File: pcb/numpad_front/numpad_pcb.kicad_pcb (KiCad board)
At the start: 2 copper layers, 81 x 160.2 mm, 63 parts, among them J1 Conn_01x16_Female

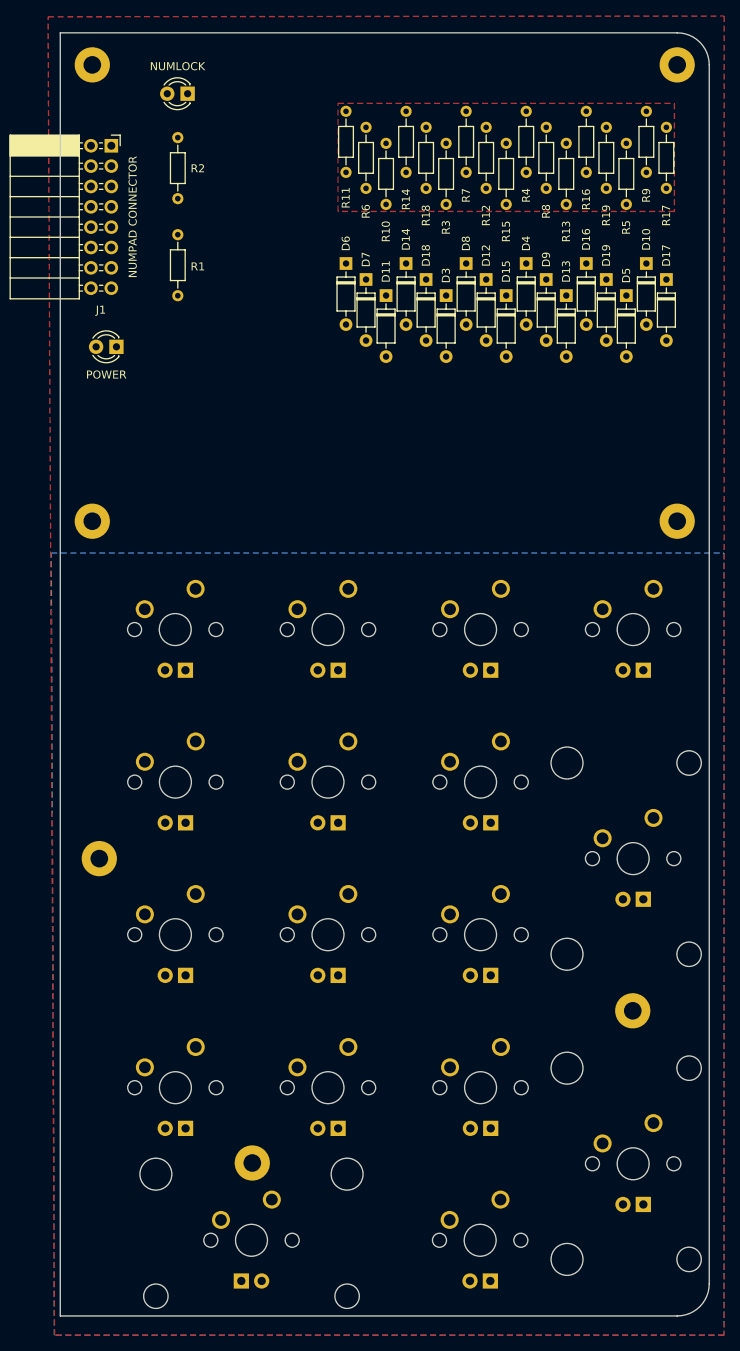
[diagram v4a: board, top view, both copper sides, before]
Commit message: Finish numpad routing
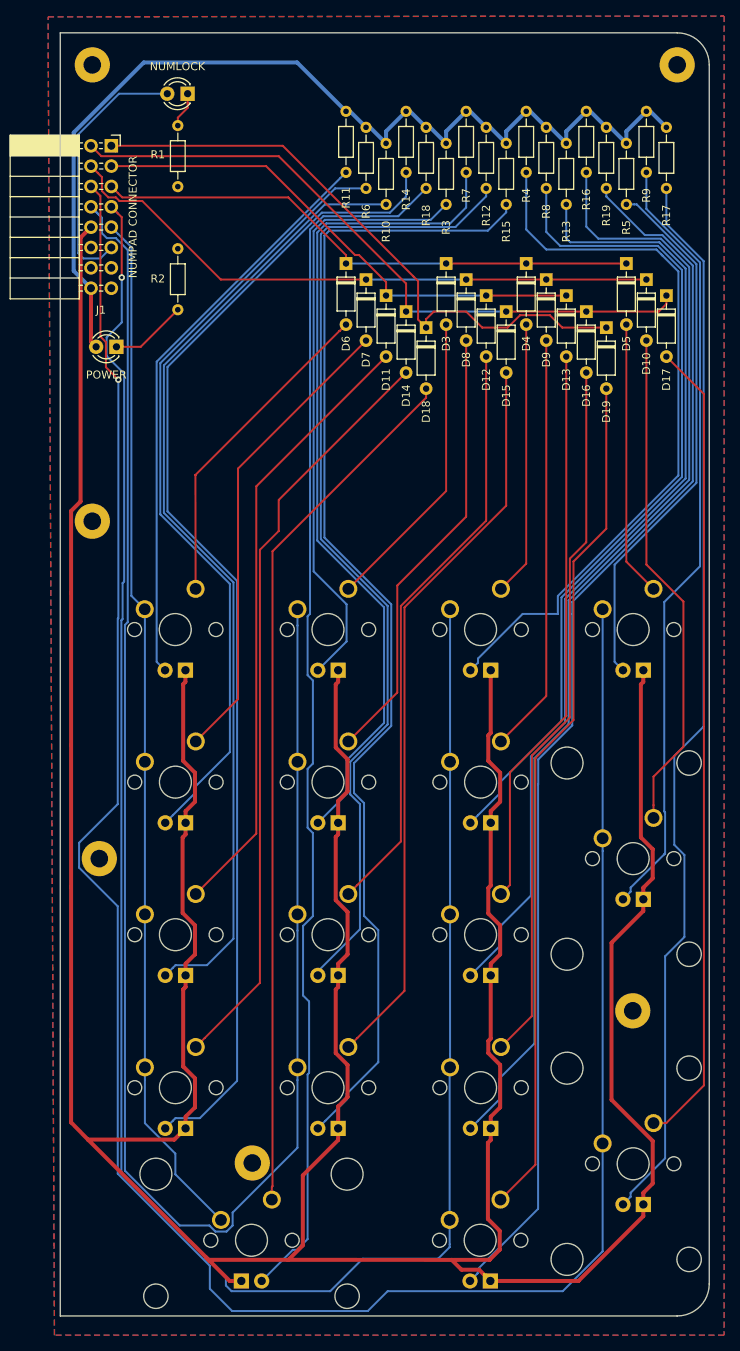
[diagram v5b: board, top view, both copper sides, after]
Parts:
- removed the REF** at (67.5, 87.0) (x2)
- added REF**: MountingHole_2.2mm_M2_Pad, MountingHole:MountingHole_2.2mm_M2_Pad, F.Cu at (67.5, 87.0)
- moved R2 6.25 mm to (78.2, 53.0), turned to 270 degrees
- moved D14 6.00 mm to (106.7, 60.8)
- moved D16 6.00 mm to (129.2, 60.8)
- moved D18 6.00 mm to (109.2, 62.8)
- moved D19 6.00 mm to (131.7, 62.8)
- moved R1 6.00 mm to (78.2, 45.2), turned to 90 degrees
- moved D3 4.00 mm to (111.7, 54.8)
- moved D5 4.00 mm to (134.2, 54.8)
- moved D10 2.00 mm to (136.7, 56.8)
- moved D12 2.00 mm to (116.7, 58.8)
- moved D15 2.00 mm to (119.2, 60.8)
- moved D17 2.00 mm to (139.2, 58.8)
- moved D8 2.00 mm to (114.2, 56.8)
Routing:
- net LEDGND: track 0.00 -> 511.9 mm
- net col19: track 0.00 -> 281.3 mm, vias 0 -> 1
- net col18: track 0.00 -> 253.9 mm, vias 0 -> 1
- net col17: track 0.00 -> 221.9 mm
- net Net-(MX17-Pad3): track 0.00 -> 153.7 mm
- net Net-(MX16-Pad3): track 0.00 -> 152.4 mm
- net Net-(MX13-Pad3): track 0.00 -> 146.1 mm
- net Net-(MX12-Pad3): track 0.00 -> 145.8 mm
- net Net-(MX14-Pad3): track 0.00 -> 140.6 mm
- net Net-(MX15-Pad3): track 0.00 -> 134.0 mm
- net +5V: track 0.00 -> 129.9 mm
- net col16: track 0.00 -> 129.7 mm
- net Net-(MX10-Pad3): track 0.00 -> 124.2 mm
- net Net-(MX9-Pad3): track 0.00 -> 121.7 mm
- net Net-(MX11-Pad3): track 0.00 -> 120.1 mm
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- added copper zone on B.Cu, net GND
- removed copper zone on F.Cu, net +5V
- removed copper zone on B.Cu, net LEDGND
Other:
- net class PWR added: clearance 0.2, trace_width 0.5, via_dia 0.8, via_drill 0.4

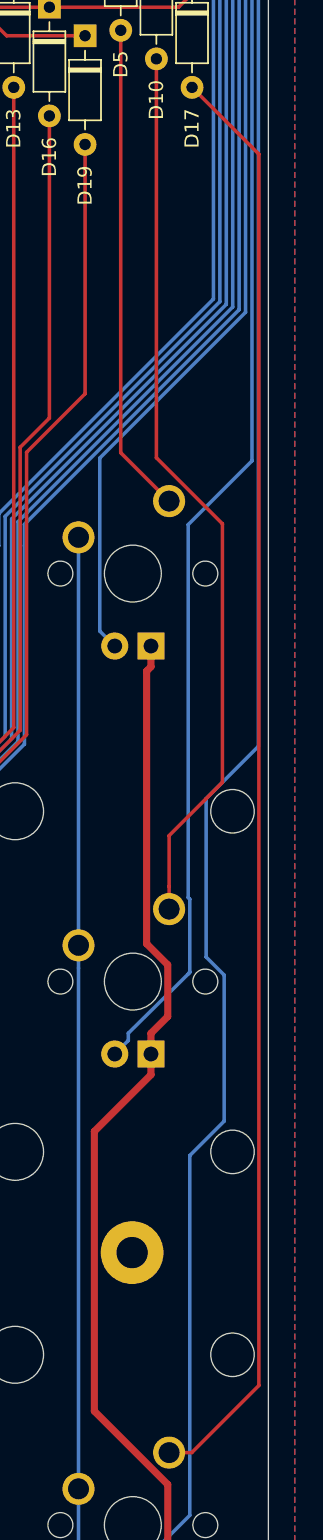
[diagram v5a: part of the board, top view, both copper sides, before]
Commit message: Rearrange main board diodes
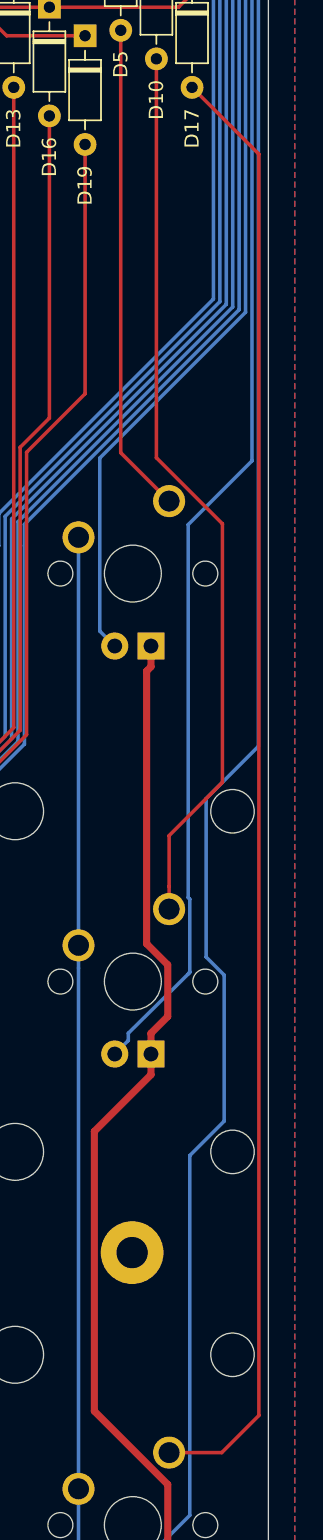
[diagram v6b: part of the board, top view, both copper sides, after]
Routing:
- net Net-(D17-Pad2): track 101.2 -> 102.4 mm
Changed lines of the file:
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@@
   (segment (start 127.15001 91.64999) (end 127.150009 111.486401) (width 0.25) (layer F.Cu) (net 22))
   (segment (start 127.150009 111.486401) (end 122.4 116.23641) (width 0.25) (layer F.Cu) (net 22))
-  (segment (start 139.18099 162.12) (end 137.59 162.12) (width 0.25) (layer F.Cu) (net 23))
-  (segment (start 143.884001 71.104001) (end 143.884001 157.416989) (width 0.25) (layer F.Cu) (net 23))
-  (segment (start 143.884001 157.416989) (end 139.18099 162.12) (width 0.25) (layer F.Cu) (net 23))
-  (segment (start 139.2 66.42) (end 143.884001 71.104001) (width 0.25) (layer F.Cu) (net 23))
+  (segment (start 143.884001 71.104001) (end 139.2 66.42) (width 0.25) (layer F.Cu) (net 23))
+  (segment (start 137.59 162.12) (end 141.28 162.12) (width 0.25) (layer F.Cu) (net 23))
+  (segment (start 143.884001 159.515999) (end 143.884001 71.104001) (width 0.25) (layer F.Cu) (net 23))
+  (segment (start 141.28 162.12) (end 143.884001 159.515999) (width 0.25) (layer F.Cu) (net 23))
   (segment (start 109.2 71.55137) (end 90.025001 90.726369) (width 0.25) (layer F.Cu) (net 24))
   (segment (start 109.2 70.42) (end 109.2 71.55137) (width 0.25) (layer F.Cu) (net 24))

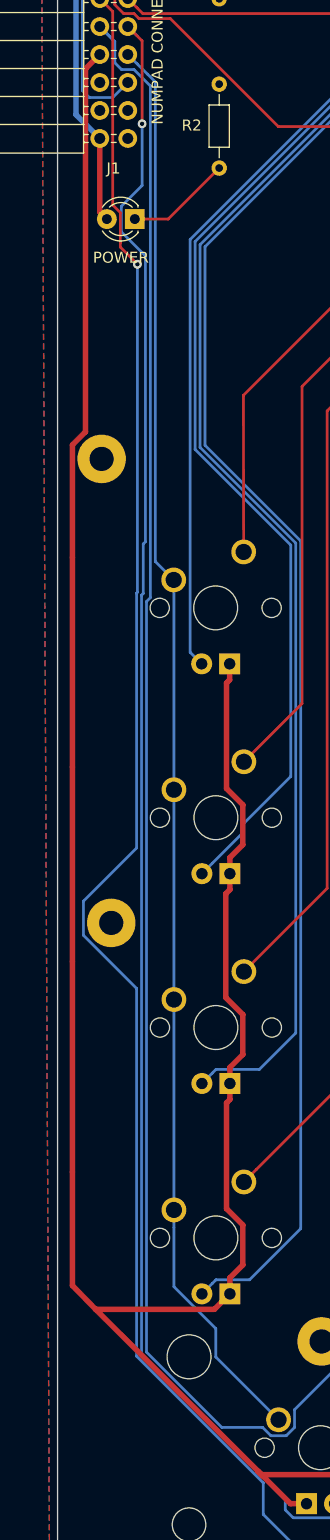
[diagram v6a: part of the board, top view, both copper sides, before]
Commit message: Finish routing main PCB
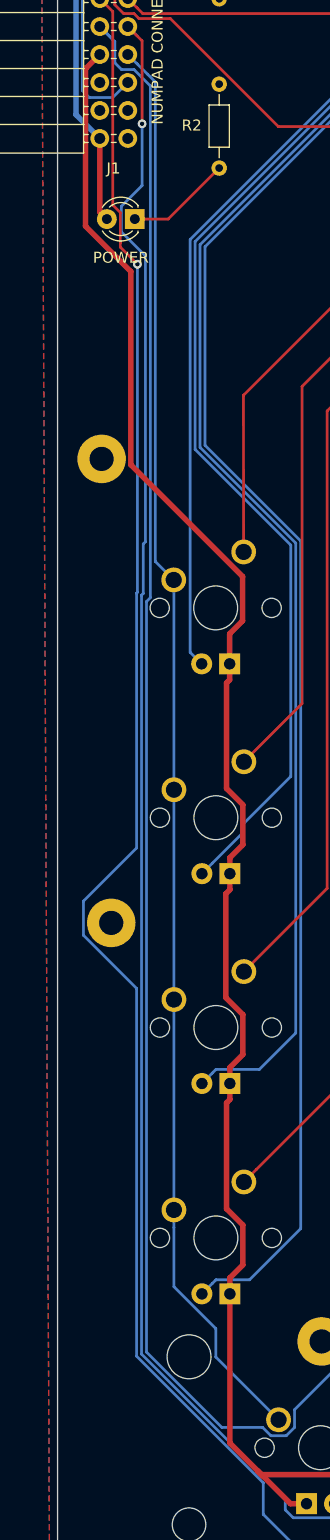
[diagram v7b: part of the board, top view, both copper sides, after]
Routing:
- net LEDGND: track 511.9 -> 441.9 mm
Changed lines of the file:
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@@
     (thickness 1.6)
     (drawings 8)
-    (tracks 579)
+    (tracks 576)
     (zones 0)
     (modules 62)
@@
   (segment (start 122.85001 167.30999) (end 118.49 171.67) (width 0.25) (layer F.Cu) (net 26))
   (segment (start 122.85001 116.54999) (end 122.85001 167.30999) (width 0.25) (layer F.Cu) (net 26))
-  (segment (start 64.874999 85.702999) (end 64.874999 95.920701) (width 0.5) (layer F.Cu) (net 31))
-  (segment (start 66.059999 84.517999) (end 64.874999 85.702999) (width 0.5) (layer F.Cu) (net 31))
-  (segment (start 66.059999 51.560001) (end 66.059999 84.517999) (width 0.5) (layer F.Cu) (net 31))
   (segment (start 67.36 50.26) (end 66.059999 51.560001) (width 0.5) (layer F.Cu) (net 31))
-  (segment (start 64.874999 95.920701) (end 64.874999 114.950701) (width 0.5) (layer F.Cu) (net 31))
-  (segment (start 64.874999 132.616001) (end 64.874999 114.950701) (width 0.5) (layer F.Cu) (net 31))
-  (segment (start 64.874999 132.616001) (end 64.874999 151.716001) (width 0.5) (layer F.Cu) (net 31))
   (segment (start 84.6775 181.83) (end 86.13 181.83) (width 0.5) (layer F.Cu) (net 31))
-  (segment (start 64.874999 151.716001) (end 64.874999 162.027499) (width 0.5) (layer F.Cu) (net 31))
   (segment (start 82.17375 179.32625) (end 84.6775 181.83) (width 0.5) (layer F.Cu) (net 31))
   (segment (start 79.17 123.1775) (end 79.17 124.63) (width 0.5) (layer F.Cu) (net 31))
@@
   (segment (start 136.32 170.8275) (end 137.493901 169.653599) (width 0.5) (layer F.Cu) (net 31))
   (segment (start 136.32 172.28) (end 136.32 170.8275) (width 0.5) (layer F.Cu) (net 31))
-  (segment (start 67.017499 164.182501) (end 67 164.2) (width 0.5) (layer F.Cu) (net 31))
-  (segment (start 79.17 162.78) (end 77.767499 164.182501) (width 0.5) (layer F.Cu) (net 31))
-  (segment (start 77.767499 164.182501) (end 67.017499 164.182501) (width 0.5) (layer F.Cu) (net 31))
-  (segment (start 64.874999 162.027499) (end 67 164.2) (width 0.5) (layer F.Cu) (net 31))
   (segment (start 93.805001 177.394999) (end 92 179.2) (width 0.5) (layer F.Cu) (net 31))
   (segment (start 93.805001 168.647499) (end 93.805001 177.394999) (width 0.5) (layer F.Cu) (net 31))
@@
   (segment (start 91.993901 179.193901) (end 92 179.2) (width 0.5) (layer F.Cu) (net 31))
   (segment (start 81.723045 178.876955) (end 82.039991 179.193901) (width 0.5) (layer F.Cu) (net 31))
-  (segment (start 67 164.2) (end 81.723045 178.876955) (width 0.5) (layer F.Cu) (net 31))
   (segment (start 118.393901 177.923073) (end 117.123073 179.193901) (width 0.5) (layer F.Cu) (net 31))
   (segment (start 113.627499 180.427499) (end 112.4 179.2) (width 0.5) (layer F.Cu) (net 31))
@@
   (segment (start 136.32 132.7275) (end 137.493901 131.553599) (width 0.5) (layer F.Cu) (net 31))
   (segment (start 136.32 134.18) (end 136.32 132.7275) (width 0.5) (layer F.Cu) (net 31))
+  (segment (start 70.175001 69.958013) (end 66.059999 65.843011) (width 0.5) (layer F.Cu) (net 31))
+  (segment (start 70.175001 87.506003) (end 70.175001 69.958013) (width 0.5) (layer F.Cu) (net 31))
+  (segment (start 80.323901 101.673073) (end 80.323901 97.654903) (width 0.5) (layer F.Cu) (net 31))
+  (segment (start 80.323901 97.654903) (end 70.175001 87.506003) (width 0.5) (layer F.Cu) (net 31))
+  (segment (start 79.15 102.846974) (end 80.323901 101.673073) (width 0.5) (layer F.Cu) (net 31))
+  (segment (start 66.059999 65.843011) (end 66.059999 51.560001) (width 0.5) (layer F.Cu) (net 31))
+  (segment (start 79.15 105.58) (end 79.15 102.846974) (width 0.5) (layer F.Cu) (net 31))
+  (segment (start 79.17 176.32391) (end 81.723045 178.876955) (width 0.5) (layer F.Cu) (net 31))
+  (segment (start 79.17 162.78) (end 79.17 176.32391) (width 0.5) (layer F.Cu) (net 31))
   (segment (start 74.09 97.98) (end 74.07 97.96) (width 0.25) (layer F.Cu) (net 32))
   (segment (start 69.9 50.26) (end 69.91 50.26) (width 0.25) (layer F.Cu) (net 32))

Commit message: Freerouting work
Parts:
- removed REF** (x6): MountingHole_2.2mm_M2_Pad, MountingHole:MountingHole_2.2mm_M2_Pad
- added MOUNT1: MountingHole_2.2mm_M2_Pad, MountingHole:MountingHole_2.2mm_M2_Pad, F.Cu at (67.5, 30.0)
- added MOUNT2: MountingHole_2.2mm_M2_Pad, MountingHole:MountingHole_2.2mm_M2_Pad, F.Cu at (140.6, 30.0)
- added MOUNT3: MountingHole_2.2mm_M2_Pad, MountingHole:MountingHole_2.2mm_M2_Pad, F.Cu at (67.5, 87.0)
- added MOUNT4: MountingHole_2.2mm_M2_Pad, MountingHole:MountingHole_2.2mm_M2_Pad, F.Cu at (140.6, 87.0)
- added MOUNT5: MountingHole_2.2mm_M2_Pad, MountingHole:MountingHole_2.2mm_M2_Pad, F.Cu at (68.4, 129.1)
- added MOUNT6: MountingHole_2.2mm_M2_Pad, MountingHole:MountingHole_2.2mm_M2_Pad, F.Cu at (135.0, 148.1)
- added MOUNT7: MountingHole_2.2mm_M2_Pad, MountingHole:MountingHole_2.2mm_M2_Pad, F.Cu at (87.5, 167.1)
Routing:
- net col19: track 281.3 -> 152.8 mm, vias 1 -> 0
- net col18: track 253.9 -> 144.2 mm, vias 1 -> 0
- net col17: track 221.9 -> 119.0 mm
- net LEDGND: track 441.9 -> 371.9 mm
- net row4: track 78.5 -> 114.7 mm
- net Net-(MX3-Pad3): track 91.6 -> 66.0 mm
- net Net-(MX7-Pad3): track 104.3 -> 84.1 mm
- net Net-(MX13-Pad3): track 146.1 -> 126.0 mm
- net +5V: track 129.9 -> 110.9 mm
- net Net-(MX11-Pad3): track 120.1 -> 102.2 mm
- net Net-(MX10-Pad3): track 124.2 -> 107.9 mm
- net Net-(MX14-Pad3): track 140.6 -> 126.6 mm
- net Net-(MX12-Pad3): track 145.8 -> 132.7 mm
- net Net-(MX9-Pad3): track 121.7 -> 109.8 mm
- net Net-(MX2-Pad3): track 75.9 -> 64.8 mm
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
